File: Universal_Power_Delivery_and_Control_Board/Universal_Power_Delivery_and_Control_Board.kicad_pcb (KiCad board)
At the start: 2 copper layers, 49 parts, among them Q2 AO4407A, Q3 AO3401A, U1 CH224Q_C46061833, U2 TPS54202DDC, U3 USBLC6-2SC6, U4 USBLC6-2SC6, U5 ESD2CAN24-ES, U6 S2B-ZR (LF)(SN), U7 TPS259470LRPWR

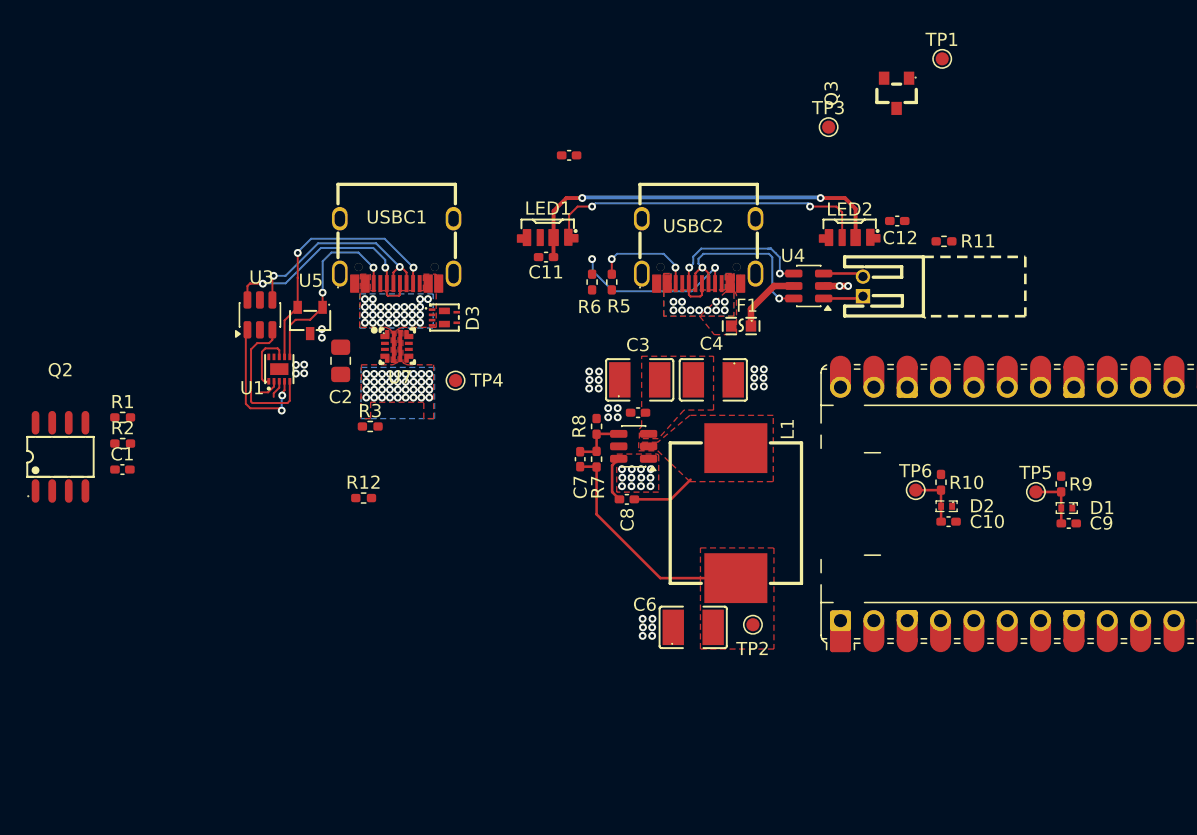
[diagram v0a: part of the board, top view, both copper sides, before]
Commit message: Imported the buck converter design block and contnued with the layout.
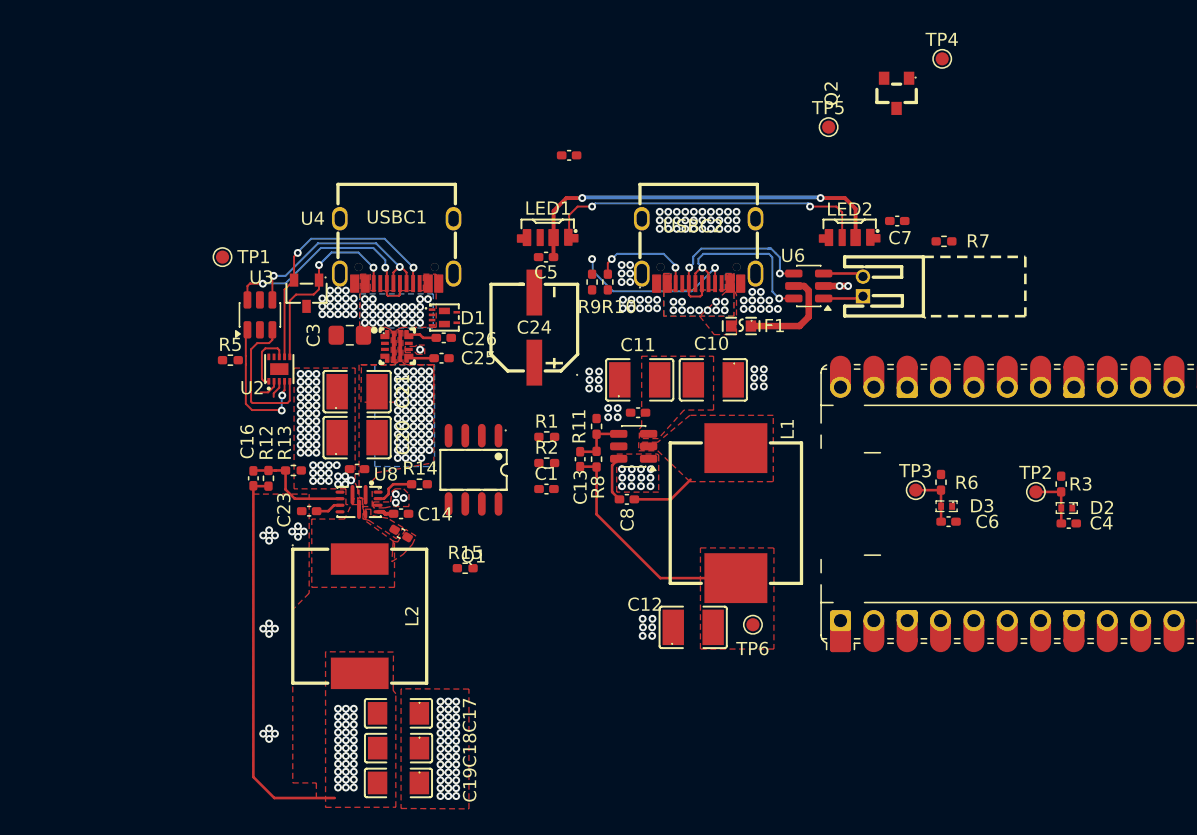
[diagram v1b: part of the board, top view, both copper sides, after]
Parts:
- removed the Q2 at (90.5, 58.2)
- added C14: 1uF, Capacitor_SMD:C_0402_1005Metric_Pad0.74x0.62mm_HandSolder, F.Cu at (116.5, 62.5)
- added C15: 100nF, Capacitor_SMD:C_0402_1005Metric_Pad0.74x0.62mm_HandSolder, F.Cu at (116.5, 64.0)
- added C16: 22pF, Capacitor_SMD:C_0402_1005Metric_Pad0.74x0.62mm_HandSolder, F.Cu at (105.2, 59.9)
- added C17: 47uF, lcsc_footprints:C426659_C1206, F.Cu at (116.2, 77.8)
- added C18: 47uF, lcsc_footprints:C426659_C1206, F.Cu at (116.3, 80.4)
- added C19: 47uF, lcsc_footprints:C426659_C1206, F.Cu at (116.2, 83.0)
- added C20: 22uF, lcsc_footprints:C778721_C1210, F.Cu at (113.1, 56.8)
- added C21: 22uF, lcsc_footprints:C778721_C1210, F.Cu at (113.1, 53.2)
- added C22: 100nF, Capacitor_SMD:C_0402_1005Metric_Pad0.74x0.62mm_HandSolder, F.Cu at (113.1, 59.1)
- added C23: ?, Capacitor_SMD:C_0402_1005Metric_Pad0.74x0.62mm_HandSolder, F.Cu at (109.5, 62.4)
- added C24: 100uF, lcsc_footprints:C19673858_CAP-SMD_BD6_3-L6_5-W6_5-LS7_2-FD_1, F.Cu at (126.6, 48.4)
- added C25: ?, Capacitor_SMD:C_0402_1005Metric_Pad0.74x0.62mm_HandSolder, F.Cu at (119.5, 50.7)
- added C26: ?, Capacitor_SMD:C_0402_1005Metric_Pad0.74x0.62mm_HandSolder, F.Cu at (119.7, 49.1)
- added L2: 1uH, lcsc_footprints:C845068_IND-SMD_L10_2-W10_2-LS10_8, F.Cu at (113.3, 70.3)
- added Q1: AO4407A, lcsc_footprints:C16072_SOIC-8_L4_9-W3_9-P1_27-LS6_0-BL, F.Cu at (122.0, 59.2)
- added R13: 20K, Resistor_SMD:R_0402_1005Metric_Pad0.72x0.64mm_HandSolder, F.Cu at (108.2, 59.2)
- added R14: 100K, Resistor_SMD:R_0402_1005Metric_Pad0.72x0.64mm_HandSolder, F.Cu at (117.8, 60.3)
- added R15: 13.3K, Resistor_SMD:R_0402_1005Metric_Pad0.72x0.64mm_HandSolder, F.Cu at (121.3, 66.7)
- added U8: TPS51385RJNR, lcsc_footprints:C22418767_QFN-12_L3_0-W2_0-P0_5-TL_NB680, F.Cu at (113.2, 61.8)
- C1: value 1nF -> ?
- R12: value 100K -> ?
- moved C1 32.3 mm to (127.5, 60.7)
- moved R1 32.3 mm to (127.5, 56.7)
- moved R2 32.3 mm to (127.5, 58.7)
- moved TP1 20.1 mm to (102.8, 43.0)
- moved R5 11.8 mm to (103.5, 50.9)
- moved R12 7.40 mm to (106.3, 59.9), turned to -90 degrees
- moved U4 2.09 mm to (109.2, 45.8)
- moved C3 2.07 mm to (112.5, 49.0), turned to 180 degrees
- moved R10 0.30 mm to (132.2, 44.9)
- renumbered C4 to C10, C3 to C11, C6 to C12, C7 to C13, C13 to C2, C2 to C3, C9 to C4, C11 to C5, C10 to C6, C12 to C7, C5 to C9, D3 to D1, D1 to D2, D2 to D3, Q3 to Q2, R5 to R10, R8 to R11, R9 to R3, R3 to R5, R10 to R6, R11 to R7, R7 to R8, R6 to R9, TP4 to TP1, TP5 to TP2, TP6 to TP3, TP1 to TP4, TP3 to TP5, TP2 to TP6, U7 to U1, U1 to U2, U5 to U4, U6 to U5, U4 to U6, U2 to U7
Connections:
- C1 pad 1: Net-(C1-Pad1) -> +12V_PD
- C1 pad 2: Net-(Q2-G) -> Net-(Q1-G)
- R1 pad 1: Net-(C1-Pad1) -> +12V_PD
- R1 pad 2: Net-(Q2-G) -> Net-(Q1-G)
- R12 pad 1: /PD_Section/PD_VBUS -> Net-(U8-FB)
- R12 pad 2: Net-(U1-CFG1) -> VOUT
- R2 pad 1: Net-(Q2-G) -> unconnected-(R2-Pad1)
- R2 pad 2: unconnected-(R2-Pad2) -> Net-(Q1-G)
- R5 pad 2: Net-(U1-CFG1) -> Net-(U2-CFG1)
- U1 pad 10: unconnected-(U7-ITIMER-Pad10) -> Net-(U1-ITIMER)
- U1 pad 3: unconnected-(U7-PG/AUXOFF-Pad3) -> /PD_Section/PG_eFUSE
- U1 pad 6: unconnected-(U7-OUT-Pad6) -> +12V_PD
- U1 pad 7: unconnected-(U7-DVDT-Pad7) -> Net-(U1-DVDT)
- U1 pad 8: unconnected-(U7-GND-Pad8) -> GND
- U1 pad 9: unconnected-(U7-ILM-Pad9) -> Net-(U1-ILM)
- U2 pad 9: Net-(U1-CFG1) -> Net-(U2-CFG1)
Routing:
- net VOUT: track 0.00 -> 30.2 mm, vias 0 -> 33
- net Net-(U8-FB): track 0.00 -> 8.35 mm
- net /TPS51385/EN_TPS51385: track 0.00 -> 3.24 mm
- net +5V_VBUS: track 5.29 -> 7.97 mm
- net Net-(U1-ITIMER): track 0.00 -> 2.20 mm
- net Net-(U8-SS): track 0.00 -> 1.97 mm
- net Net-(U1-DVDT): track 0.00 -> 1.92 mm
- net Net-(U8-VCC): track 0.00 -> 1.24 mm
- net unconnected-(U7-OUT-Pad6): vias 36 -> 0
- net GND: vias 42 -> 218
- net +12V_PD: vias 0 -> 59
- added copper zone on B.Cu, net +12V_PD
- added copper zone on F.Cu, net +12V_PD
- added copper zone on F.Cu, net Net-(U8-SW)
- added copper zone on F.Cu, net Net-(U8-VBST)
- added copper zone on F.Cu, net VOUT
- removed copper zone on B.Cu, net unconnected-(U7-OUT-Pad6)
- removed copper zone on F.Cu, net unconnected-(U7-OUT-Pad6)
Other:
- board text added: "Coil Keep Out"
- board text added: "TYPE-C-31-M-12"

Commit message: Finally figured out the soft start circuitry.
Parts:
- removed C1: ?, Capacitor_SMD:C_0402_1005Metric_Pad0.74x0.62mm_HandSolder
- removed Q1: AO4407A, lcsc_footprints:C16072_SOIC-8_L4_9-W3_9-P1_27-LS6_0-BL
- removed R1: 10K, Resistor_SMD:R_0402_1005Metric_Pad0.72x0.64mm_HandSolder
- removed R2: 1K, Resistor_SMD:R_0402_1005Metric_Pad0.72x0.64mm_HandSolder
- added C27: 160nF, Capacitor_SMD:C_0402_1005Metric_Pad0.74x0.62mm_HandSolder, F.Cu at (122.3, 66.5)
- added CN1: B03B-XASK-1-A(LF)(SN), lcsc_footprints:C264992_CONN-TH_B03B-XASK-1-A-LF-SN, F.Cu at (146.0, 78.0)
- added CN2: B03B-XASK-1-A(LF)(SN), lcsc_footprints:C264992_CONN-TH_B03B-XASK-1-A-LF-SN, F.Cu at (138.3, 78.0)
- added CN3: B03B-XASK-1-A(LF)(SN), lcsc_footprints:C264992_CONN-TH_B03B-XASK-1-A-LF-SN, F.Cu at (130.7, 78.0)
- added CN4: B03B-XASK-1-A(LF)(SN), lcsc_footprints:C264992_CONN-TH_B03B-XASK-1-A-LF-SN, F.Cu at (123.0, 78.0)
- added R16: 1K, Resistor_SMD:R_0402_1005Metric_Pad0.72x0.64mm_HandSolder, F.Cu at (123.5, 68.2)
- added R17: 10K, Resistor_SMD:R_0402_1005Metric_Pad0.72x0.64mm_HandSolder, F.Cu at (126.0, 68.2)
- added U9: TPS24751RUVR, lcsc_footprints:C2653596_VQFN-36_L7_0-W3_5-P0_50-BL-EP, F.Cu at (125.0, 63.6)
- moved R15 14.8 mm to (120.5, 52.0)
- moved C19 5.47 mm to (112.8, 78.8), turned to 90 degrees
- moved R7 3.51 mm to (154.3, 41.6)
- moved C17 2.11 mm to (118.0, 78.8), turned to 90 degrees
- moved TP1 2.09 mm to (103.2, 45.0)
- moved C18 1.76 mm to (115.4, 78.9), turned to 90 degrees
- moved R5 1.32 mm to (103.7, 52.1), turned to 90 degrees
- moved C11 1.25 mm to (135.5, 51.5), turned to -90 degrees
- moved C24 1.22 mm to (126.0, 49.4)
- moved A1 1.06 mm to (174.0, 60.7)
- moved R14 0.45 mm to (117.8, 60.8), turned to -90 degrees
- moved C7 0.26 mm to (154.3, 40.5)
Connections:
- net /TPS51385/EN_TPS51385 renamed /Power_Output/EN_TPS51385
- net /TPS51385/MODE_TPS51385 renamed /Power_Output/MODE_TPS51385
- net /TPS51385/PG_TPS51385 renamed /Power_Output/PG_TPS51385
- net VOUT renamed VOUT_connectors
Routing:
- net /PD_Section/SCL: track 1.60 -> 34.8 mm, vias 0 -> 2
- net /PD_Section/SDA: track 1.37 -> 34.3 mm, vias 0 -> 2
- net /PD_Section/PD_VBUS: track 4.69 -> 24.9 mm, vias 28 -> 31
- net VOUT_connectors: track 30.2 -> 24.3 mm, vias 33 -> 32
- net Net-(U2-CFG1): track 0.00 -> 4.85 mm, vias 0 -> 2
- net +12V_PD: track 0.00 -> 4.07 mm
- net GND: track 1.86 -> 5.04 mm, vias 218 -> 225
- net Net-(U9-GATE): track 0.00 -> 2.96 mm
- net +5V_VSYS: track 29.5 -> 32.2 mm
- net Net-(C27-Pad2): track 0.00 -> 1.67 mm
- net /Power_Output/SOFT_START_EN: track 0.00 -> 1.55 mm
- net Net-(LED2-DIN): track 0.00 -> 1.35 mm
- net Net-(U2-CC2): track 15.0 -> 15.7 mm
- net /Power_Output/EN_TPS51385: track 3.24 -> 3.90 mm

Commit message: Restructured the schematic, added the digital output section and continued with the layout.
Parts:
- added C28: 100nF, Capacitor_SMD:C_0402_1005Metric_Pad0.74x0.62mm_HandSolder, F.Cu at (252.0, 50.6)
- added C29: 100nF, Capacitor_SMD:C_0402_1005Metric_Pad0.74x0.62mm_HandSolder, F.Cu at (252.0, 52.5)
- added C30: 100nF, Capacitor_SMD:C_0402_1005Metric_Pad0.74x0.62mm_HandSolder, F.Cu at (252.0, 54.5)
- added C31: 100nF, Capacitor_SMD:C_0402_1005Metric_Pad0.74x0.62mm_HandSolder, F.Cu at (252.0, 56.5)
- added C32: 100nF, Capacitor_SMD:C_0402_1005Metric_Pad0.74x0.62mm_HandSolder, F.Cu at (252.0, 58.5)
- added FPC1: XW05202-100R-00, lcsc_footprints:C2906114_FPC-SMD_10P-P0_50_HCTL_XW05202-100R-00, F.Cu at (255.9, 44.5)
- added FPC2: XW05202-100R-00, lcsc_footprints:C2906114_FPC-SMD_10P-P0_50_HCTL_XW05202-100R-00, F.Cu at (139.5, 101.3)
- added FPC3: XW05202-100R-00, lcsc_footprints:C2906114_FPC-SMD_10P-P0_50_HCTL_XW05202-100R-00, F.Cu at (150.5, 101.3)
- added FPC4: XW05202-100R-00, lcsc_footprints:C2906114_FPC-SMD_10P-P0_50_HCTL_XW05202-100R-00, F.Cu at (230.4, 59.8)
- added FPC5: XW05202-100R-00, lcsc_footprints:C2906114_FPC-SMD_10P-P0_50_HCTL_XW05202-100R-00, F.Cu at (230.5, 67.3)
- added FPC6: XW05202-100R-00, lcsc_footprints:C2906114_FPC-SMD_10P-P0_50_HCTL_XW05202-100R-00, F.Cu at (230.5, 74.9)
- added FPC7: XW05202-100R-00, lcsc_footprints:C2906114_FPC-SMD_10P-P0_50_HCTL_XW05202-100R-00, F.Cu at (230.5, 82.5)
- added JP1: SolderJumper_2_Open, Jumper:SolderJumper-2_P1.3mm_Open_RoundedPad1.0x1.5mm, F.Cu at (140.2, 71.1)
- added JP2: SolderJumper_2_Open, Jumper:SolderJumper-2_P1.3mm_Open_RoundedPad1.0x1.5mm, F.Cu at (142.9, 71.1)
- added JP3: SolderJumper_2_Open, Jumper:SolderJumper-2_P1.3mm_Open_RoundedPad1.0x1.5mm, F.Cu at (145.6, 71.1)
- added JP4: SolderJumper_2_Open, Jumper:SolderJumper-2_P1.3mm_Open_RoundedPad1.0x1.5mm, B.Cu at (156.8, 77.5)
- added R18: 33R, Resistor_SMD:R_0402_1005Metric_Pad0.72x0.64mm_HandSolder, F.Cu at (255.2, 54.7)
- added RN1: YC164-JR-0733RL, lcsc_footprints:C165956_RES-ARRAY-SMD_0603-8P-L3_2-W1_6-BL, F.Cu at (256.1, 51.7)
- added RN2: YC164-JR-0733RL, lcsc_footprints:C165956_RES-ARRAY-SMD_0603-8P-L3_2-W1_6-BL, F.Cu at (140.1, 96.0)
- added RN3: YC164-JR-0733RL, lcsc_footprints:C165956_RES-ARRAY-SMD_0603-8P-L3_2-W1_6-BL, F.Cu at (149.8, 96.0)
- added U10: SN74LVC1G17DCKR, lcsc_footprints:C10425_SC-70-5_L2_1-W1_3-P0_65-LS2_1-BR, F.Cu at (248.3, 43.8)
- added U11: SN74LVC1G17DCKR, lcsc_footprints:C10425_SC-70-5_L2_1-W1_3-P0_65-LS2_1-BR, F.Cu at (248.3, 47.6)
- added U12: SN74LVC1G17DCKR, lcsc_footprints:C10425_SC-70-5_L2_1-W1_3-P0_65-LS2_1-BR, F.Cu at (248.3, 51.4)
- added U13: SN74LVC1G17DCKR, lcsc_footprints:C10425_SC-70-5_L2_1-W1_3-P0_65-LS2_1-BR, F.Cu at (248.3, 55.2)
- added U14: SN74LVC1G17DCKR, lcsc_footprints:C10425_SC-70-5_L2_1-W1_3-P0_65-LS2_1-BR, F.Cu at (248.3, 59.0)
- added U15: SN74LVC541APWR_C113281, lcsc_footprints:C113281_TSSOP-20_L6_5-W4_4-P0_65-LS6_4-BL, F.Cu at (145.5, 89.1)
- moved CN4 28.9 mm to (151.9, 78.7)
- moved R3 24.7 mm to (191.4, 58.8)
- moved R6 24.7 mm to (182.2, 58.7)
- moved C4 24.7 mm to (192.0, 61.8)
- moved C6 24.7 mm to (182.8, 61.7)
- moved D2 24.7 mm to (191.8, 60.6)
- moved D3 24.7 mm to (182.7, 60.5)
- moved TP2 24.7 mm to (189.5, 59.4)
- moved TP3 24.7 mm to (180.3, 59.3)
- moved CN1 16.4 mm to (129.6, 78.7)
- moved CN3 13.8 mm to (144.5, 78.7)
- moved C12 12.8 mm to (150.3, 66.0), turned to 180 degrees
- moved TP6 3.56 mm to (146.3, 69.2)
- moved CN2 1.47 mm to (137.0, 78.7)
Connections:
- net Net-(Q2-S) renamed TPS54202_OUTPUT
- A1 pad 13: Net-(A1-GND-Pad13) -> GND
- A1 pad 18: Net-(A1-GND-Pad13) -> GND
- A1 pad 23: Net-(A1-GND-Pad13) -> GND
- A1 pad 28: Net-(A1-GND-Pad13) -> GND
- A1 pad 3: Net-(A1-GND-Pad13) -> GND
- A1 pad 33: unconnected-(A1-AGND-Pad33) -> GND
- A1 pad 36: unconnected-(A1-3V3-Pad36) -> +3V3
- A1 pad 38: Net-(A1-GND-Pad13) -> GND
- A1 pad 8: Net-(A1-GND-Pad13) -> GND
- CN1 pad 1: VOUT_connectors -> GND
- CN1 pad 2: unconnected-(CN1-Pad2) -> Net-(CN1-Pad2)
- CN1 pad 3: GND -> VOUT_connectors
- CN2 pad 1: VOUT_connectors -> GND
- CN2 pad 2: unconnected-(CN2-Pad2) -> Net-(CN2-Pad2)
- CN2 pad 3: GND -> VOUT_connectors
- CN3 pad 1: VOUT_connectors -> GND
- CN3 pad 2: unconnected-(CN3-Pad2) -> Net-(CN3-Pad2)
- CN3 pad 3: GND -> VOUT_connectors
- CN4 pad 1: VOUT_connectors -> GND
- CN4 pad 2: unconnected-(CN4-Pad2) -> Net-(JP4-B)
- CN4 pad 3: GND -> VOUT_connectors
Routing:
- net Net-(CN1-Pad2): track 0.00 -> 27.1 mm
- net Net-(CN2-Pad2): track 0.00 -> 19.4 mm
- net Net-(CN3-Pad2): track 0.00 -> 14.0 mm, vias 0 -> 1
- net Net-(JP4-B): track 0.00 -> 3.75 mm, vias 0 -> 13
- net VOUT_connectors: vias 32 -> 33
- net GND: vias 225 -> 224
- net +3V3: vias 0 -> 18
- added copper zone on B.Cu, net +3V3
- added copper zone on F.Cu, net +3V3
- added copper zone on B.Cu, net Net-(JP4-B)
- added copper zone on F.Cu, net Net-(JP4-B)
